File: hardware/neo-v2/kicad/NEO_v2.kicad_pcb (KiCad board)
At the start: 4 copper layers, 84 x 89 mm, 500 parts, among them J1 ST-PJ-930A, J2 WY-3315, J201 OLED I2C, Q1 CJ3407, Q10 LBSS138WT1G, Q2 LBSS138WT1G, Q201 FS8205A, Q202 FS8205A, Q203 CSD25402Q3A, Q3 LBSS138WT1G, Q4 S9013W, Q6 LBSS138WT1G, SW1 SK-22H07, SW2 AN-P1S-2SP-Z, SW201 MSK-22D18G3, SW3 MK-12C02 G1.5, U1 ESP32-S3R8, U10 TPS62827DMQR, U11 ME6211C18M5G-N, U12 TPS62065DSGR, U14 SN74LVC1G17DCKR, U15 ZB25VQ128DSJG, U16 W25Q256JVEIQ, U17 SGM7222YWQ10/TR, U18 SGM2036S-3.3XXDH4G/TR, U19 LC1458CB5TR33, U2 XU316-1024-QF60B-C24​, U201 TPS2121RUXR, U202 TPS61022RWUT, U203 BQ25170DSGR, U204 MAX17048G+T10, U205 DW01A, U206 LM66200DRLR, U3 ZB25VQ32DSJG, U4 MSM261DHP006, U5 MSM261DHP006, U6 SN74LVC125APWR, U7 SN74LVC1G17DCKR, U8 TLV320AIC3204IRHBR, U9 TPA6211A1DGNR, X1 24MHz 12pF, X2 40MHz

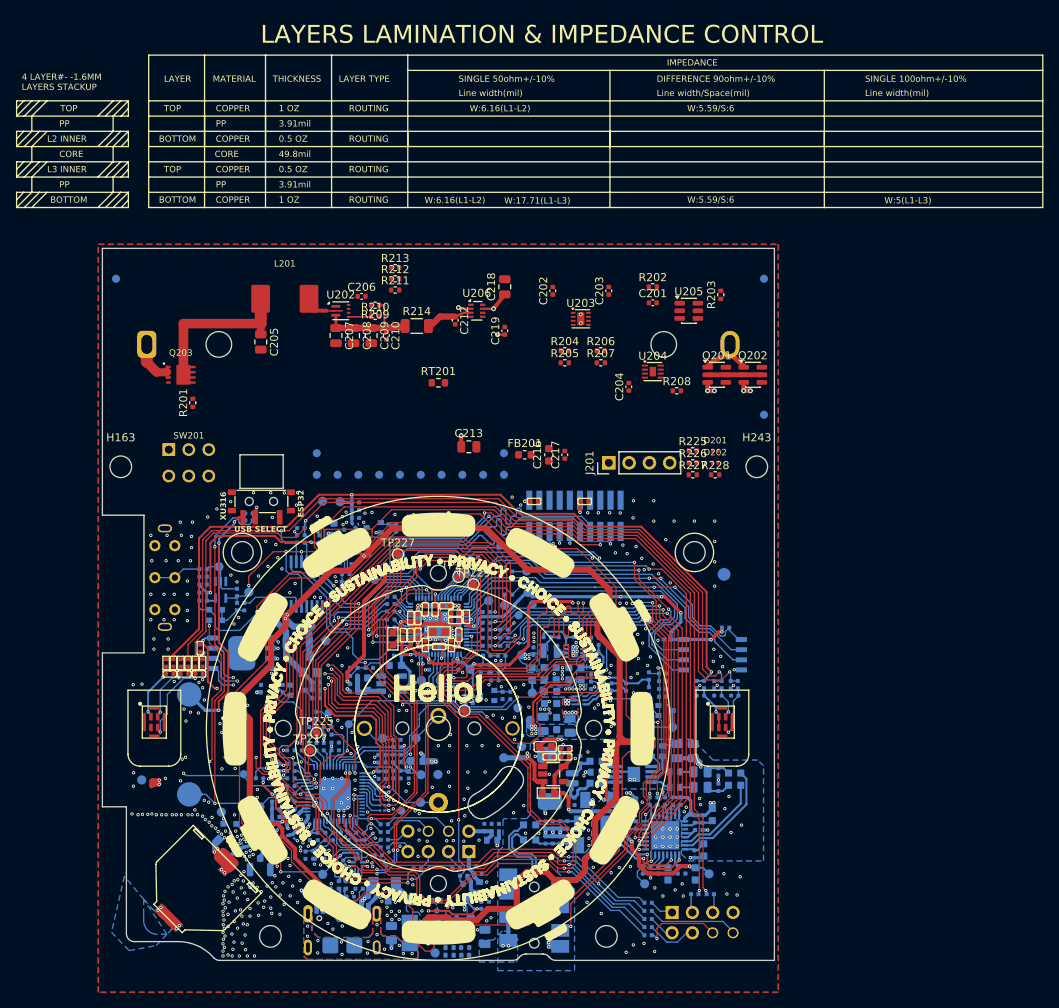
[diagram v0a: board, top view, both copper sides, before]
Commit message: NEO v2 fase 5: ruteo completo, ERC y DRC sin errores
- Router A* propio (tools/route_signals.py) en lugar de Freerouting, que
  no convergía y no garantiza respetar el cobre heredado: 71 conexiones,
  ~1225 mm y 56 vías nuevas, sin tocar cobre existente.
- Potencia y lazos críticos a mano (route_power.py); elevador recolocado
  con COUT junto a VOUT/GND; escapes de U201 y U203 reordenados.
- Cosido de GND en la franja y unión de bolsas aisladas (stitch_gnd.py).
- Retiradas R220 (OVP de U201: sin camino en el PCB heredado; protección
  igual que el original) y C214 (redundante con C83).
- ERC: 0 errores (anotaciones PWR_FLAG/no conexión en hojas heredadas).
- DRC con paridad: 0 violaciones, 0 pendientes; 8 errores del original
  como exclusiones comentadas (drc_exclusions.py).
- build_pcb.sh reconstruye el PCB de forma reproducible desde el original.
- docs/fase5-ruteo.md, renders, BOM de bloques nuevos, cálculos, CHANGES.

Co-Authored-By: Claude Opus 5.5 <noreply@anthropic.com>
Claude-Session: https://claude.ai/code/session_01UWwWJAyCeb1aBHbGbkDaMx
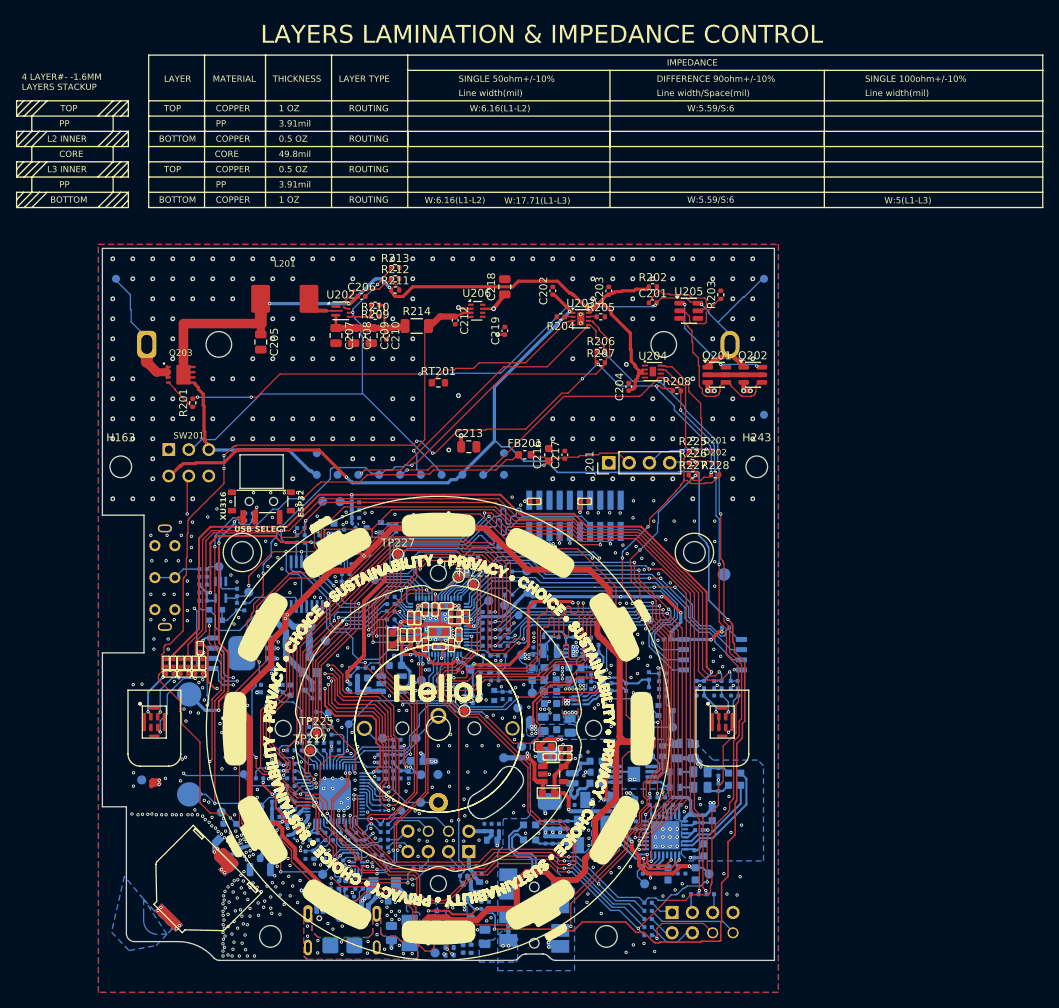
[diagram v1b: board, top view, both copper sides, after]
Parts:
- removed C214: 100nF, Capacitor_SMD:C_0402_1005Metric
- removed R220: 43.2k, Resistor_SMD:R_0402_1005Metric
- moved R205 7.30 mm to (223.5, 24.8)
- moved R204 4.28 mm to (218.5, 24.8), turned to 180 degrees
- moved C215 0.84 mm to (206.3, 103.8), turned to -90 degrees
- moved R222 0.76 mm to (207.3, 103.8), turned to -90 degrees
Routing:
- net VBUS: track 13.8 -> 203.9 mm, vias 3 -> 6
- net ESP_3V3: track 77.2 -> 211.6 mm, vias 9 -> 18
- net ESP_IO42: track 51.3 -> 179.9 mm, vias 2 -> 6
- net ESP_IO48: track 46.5 -> 160.6 mm, vias 2 -> 6
- net /Alimentacion/PACK_P: track 18.4 -> 106.6 mm, vias 0 -> 3
- net CHG_PG: track 33.3 -> 120.8 mm, vias 3 -> 6
- net /Alimentacion/SW_OV1: track 0.00 -> 81.3 mm, vias 0 -> 6
- net /Alimentacion/CELL_N: track 5.43 -> 84.5 mm, vias 0 -> 5
- net /Alimentacion/BOOST_EN: track 0.00 -> 55.6 mm, vias 0 -> 2
- net I2C_SCL: track 107.5 -> 148.8 mm, vias 6 -> 8
- net I2C_SDA: track 109.2 -> 148.2 mm, vias 6 -> 8
- net +3V3: track 160.3 -> 199.3 mm, vias 20 -> 21
- net /Alimentacion/CHG_TS: track 0.00 -> 20.2 mm
- net /Alimentacion/DW_OC: track 0.00 -> 19.0 mm
- net /Alimentacion/BOOST_5V: track 5.48 -> 23.7 mm, vias 0 -> 1
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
